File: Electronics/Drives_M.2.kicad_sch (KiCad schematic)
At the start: 87 parts, among them IC3 LM61480Q3RPHRQ1, J14 Bus_M.2_Socket_M, J15 Bus_M.2_Socket_M, J16 Bus_M.2_Socket_M, J17 Bus_M.2_Socket_M, M1 M.2 Screw, M10 M.2 Solder Nut, M11 M.2 Screw, M12 M.2 Screw, M13 M.2 Solder Nut, M14 M.2 Solder Nut, M15 M.2 Solder Nut, M16 M.2 Solder Nut, M17 M.2 Solder Nut, M18 M.2 Solder Nut, M19 M.2 Solder Nut, M2 M.2 Screw, M20 M.2 Solder Nut, M3 M.2 Solder Nut, M4 M.2 Solder Nut, M5 M.2 Solder Nut, M6 M.2 Solder Nut, M7 M.2 Solder Nut, M8 M.2 Solder Nut, M9 M.2 Solder Nut, U7 ASEK-32.768KHZ-L-R-T, U8 ASM1184

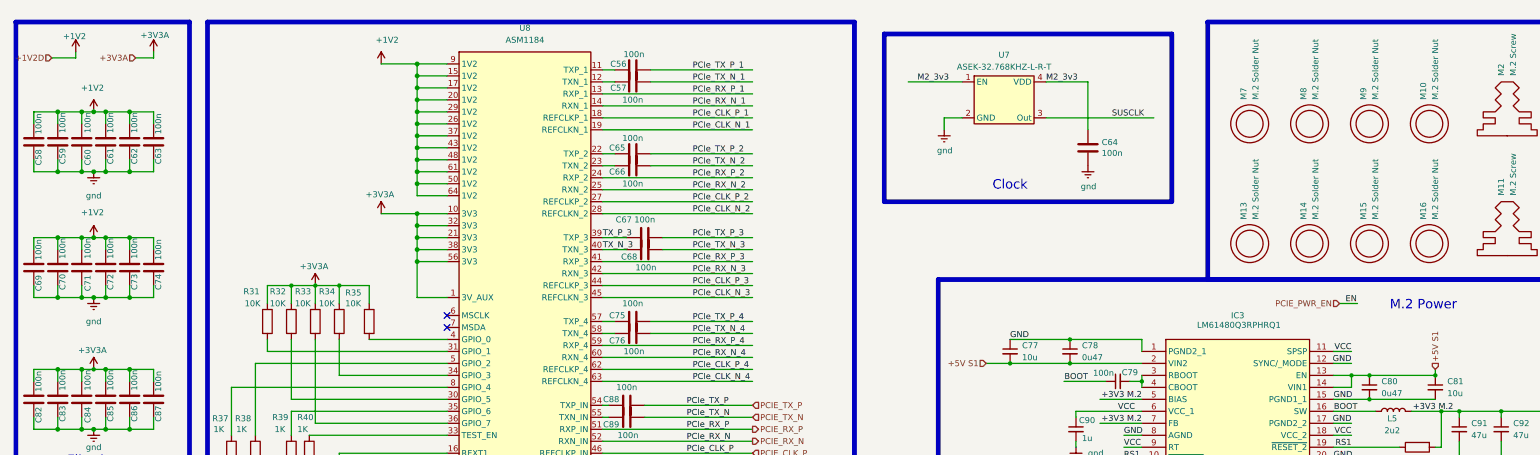
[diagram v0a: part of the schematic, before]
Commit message: Power symbols changed and sata hub fixed schem
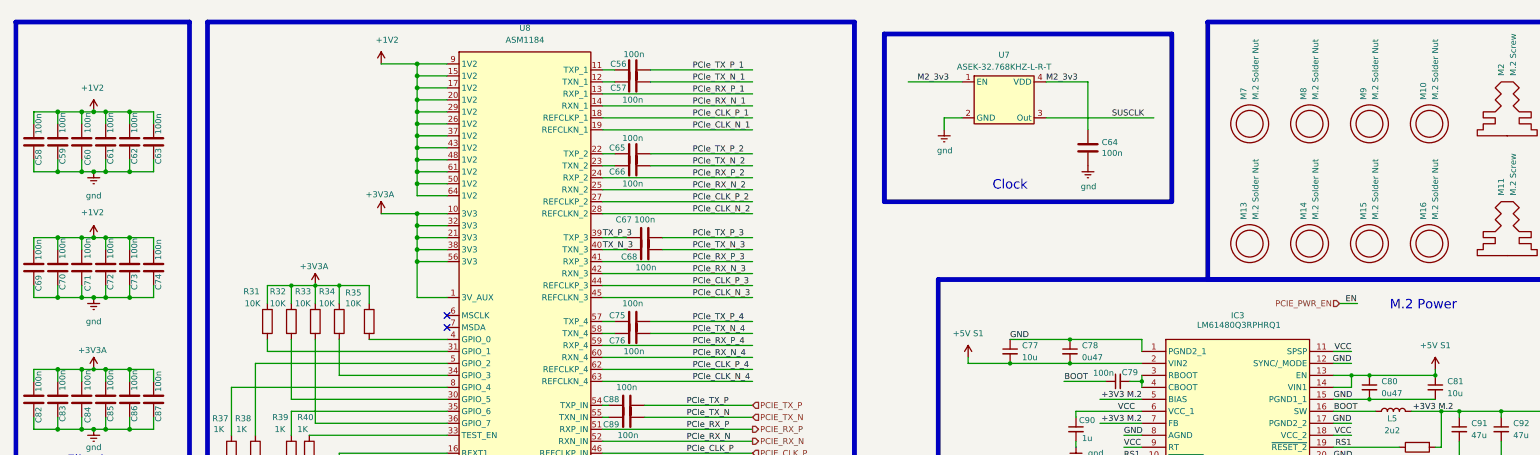
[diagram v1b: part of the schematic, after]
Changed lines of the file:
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@@
 	(wire
 		(pts
-			(xy 38.1 21.59) (xy 41.91 21.59)
-		)
-		(stroke
-			(width 0)
-			(type default)
-		)
-	)
-	(wire
-		(pts
 			(xy 87.63 81.28) (xy 104.14 81.28)
 		)
@@
 	(wire
 		(pts
-			(xy 25.4 21.59) (xy 25.4 20.32)
-		)
-		(stroke
-			(width 0)
-			(type default)
-		)
-	)
-	(wire
-		(pts
 			(xy 125.73 144.78) (xy 138.43 144.78)
 		)
@@
 	(wire
 		(pts
-			(xy 41.91 21.59) (xy 41.91 20.32)
+			(xy 137.16 67.31) (xy 168.91 67.31)
 		)
 		(stroke
@@
 	(wire
 		(pts
-			(xy 137.16 67.31) (xy 168.91 67.31)
+			(xy 214.63 85.09) (xy 214.63 86.36)
 		)
 		(stroke
@@
 	(wire
 		(pts
+			(xy 214.63 86.36) (xy 223.52 86.36)
+		)
+		(stroke
+			(width 0)
+			(type default)
+		)
+	)
+	(wire
+		(pts
 			(xy 223.52 81.28) (xy 236.22 81.28)
 		)
@@
 	(wire
 		(pts
-			(xy 20.32 21.59) (xy 25.4 21.59)
-		)
-		(stroke
-			(width 0)
-			(type default)
-		)
-	)
-	(wire
-		(pts
 			(xy 81.28 116.84) (xy 81.28 115.57)
 		)
@@
 	(wire
 		(pts
-			(xy 218.44 86.36) (xy 223.52 86.36)
-		)
-		(stroke
-			(width 0)
-			(type default)
-		)
-	)
-	(wire
-		(pts
 			(xy 125.73 162.56) (xy 138.43 162.56)
 		)
@@
 		)
 	)
-	(hierarchical_label "+3V3A"
-		(shape input)
-		(at 38.1 21.59 180)
-		(effects
-			(font
-				(size 1.27 1.27)
-			)
-			(justify right)
-		)
-	)
 	(hierarchical_label "PCIE_nCLKREQ"
 		(shape bidirectional)
@@
 		)
 	)
-	(hierarchical_label "+5V S1"
-		(shape input)
-		(at 313.69 87.63 90)
-		(effects
-			(font
-				(size 1.27 1.27)
-			)
-			(justify left)
-		)
-	)
 	(hierarchical_label "PCIE_nWAKE"
 		(shape bidirectional)
@@
 		)
 	)
-	(hierarchical_label "+5V S1"
-		(shape input)
-		(at 218.44 86.36 180)
-		(effects
-			(font
-				(size 1.27 1.27)
-			)
-			(justify right)
-		)
-	)
 	(hierarchical_label "PCIE_nWAKE"
 		(shape bidirectional)
@@
 		)
 	)
-	(hierarchical_label "+1V2D"
-		(shape input)
-		(at 20.32 21.59 180)
-		(effects
-			(font
-				(size 1.27 1.27)
-			)
-			(justify right)
-		)
-	)
 	(rule_area
 		(polyline
@@
 	)
 	(symbol
+		(lib_id "power:+5V")
+		(at 214.63 85.09 0)
+		(unit 1)
+		(exclude_from_sim no)
+		(in_bom yes)
+		(on_board yes)
+		(dnp no)
+		(fields_autoplaced yes)
+		(property "Reference" "#PWR051"
+			(at 214.63 88.9 0)
+			(effects
+				(font
+					(size 1.27 1.27)
+				)
+				(hide yes)
+			)
+		)
+		(property "Value" "+5V S1"
+			(at 214.63 80.01 0)
+			(effects
+				(font
+					(size 1.27 1.27)
+				)
+			)
+		)
+		(property "Footprint" ""
+			(at 214.63 85.09 0)
+			(effects
+				(font
+					(size 1.27 1.27)
+				)
+				(hide yes)
+			)
+		)
+		(property "Datasheet" ""
+			(at 214.63 85.09 0)
+			(effects
+				(font
+					(size 1.27 1.27)
+				)
+				(hide yes)
+			)
+		)
+		(property "Description" "Power symbol creates a global label with name \"+5V\""
+			(at 214.63 85.09 0)
+			(effects
+				(font
+					(size 1.27 1.27)
+				)
+				(hide yes)
+			)
+		)
+		(pin "1"
+		)
+		(instances
+			(project "CM5 Nas"
+				(path "/0650c7a8-acba-429c-9f8e-eec0baf0bc1c/fede4c36-00cc-4d3d-b71c-5243ba232202/3838f96b-aabd-4e80-8b25-6301712882d2"
+					(reference "#PWR051")
+					(unit 1)
+				)
+			)
+		)
+	)
+	(symbol
 		(lib_id "power:Earth")
 		(at 67.31 110.49 0)
@@
 	)
 	(symbol
-		(lib_id "power:+1V2")
-		(at 25.4 20.32 0)
-		(unit 1)
-		(exclude_from_sim no)
-		(in_bom yes)
-		(on_board yes)
-		(dnp no)
-		(property "Reference" "#PWR051"
-			(at 25.4 24.13 0)
-			(effects
-				(font
-					(size 1.27 1.27)
-				)
-				(hide yes)
-			)
-		)
-		(property "Value" "+1V2"
-			(at 25.146 17.018 0)
-			(effects
-				(font
-					(size 1.27 1.27)
-				)
-			)
-		)
-		(property "Footprint" ""
-			(at 25.4 20.32 0)
-			(effects
-				(font
-					(size 1.27 1.27)
-				)
-				(hide yes)
-			)
-		)
-		(property "Datasheet" ""
-			(at 25.4 20.32 0)
-			(effects
-				(font
-					(size 1.27 1.27)
-				)
-				(hide yes)
-			)
-		)
-		(property "Description" ""
-			(at 25.4 20.32 0)
-			(effects
-				(font
-					(size 1.27 1.27)
-				)
-			)
-		)
-		(pin "1"
-		)
-		(instances
-			(project "CM5 Nas"
-				(path "/0650c7a8-acba-429c-9f8e-eec0baf0bc1c/fede4c36-00cc-4d3d-b71c-5243ba232202/3838f96b-aabd-4e80-8b25-6301712882d2"
-					(reference "#PWR051")
-					(unit 1)
-				)
-			)
-		)
-	)
-	(symbol
 		(lib_id "Device:C")
 		(at 21.59 93.98 0)
@@
 	)
 	(symbol
+		(lib_id "power:+5V")
+		(at 313.69 87.63 0)
+		(unit 1)
+		(exclude_from_sim no)
+		(in_bom yes)
+		(on_board yes)
+		(dnp no)
+		(fields_autoplaced yes)
+		(property "Reference" "#PWR052"
+			(at 313.69 91.44 0)
+			(effects
+				(font
+					(size 1.27 1.27)
+				)
+				(hide yes)
+			)
+		)
+		(property "Value" "+5V S1"
+			(at 313.69 82.55 0)
+			(effects
+				(font
+					(size 1.27 1.27)
+				)
+			)
+		)
+		(property "Footprint" ""
+			(at 313.69 87.63 0)
+			(effects
+				(font
+					(size 1.27 1.27)
+				)
+				(hide yes)
+			)
+		)
+		(property "Datasheet" ""
+			(at 313.69 87.63 0)
+			(effects
+				(font
+					(size 1.27 1.27)
+				)
+				(hide yes)
+			)
+		)
+		(property "Description" "Power symbol creates a global label with name \"+5V\""
+			(at 313.69 87.63 0)
+			(effects
+				(font
+					(size 1.27 1.27)
+				)
+				(hide yes)
+			)
+		)
+		(pin "1"
+		)
+		(instances
+			(project "CM5 Nas"
+				(path "/0650c7a8-acba-429c-9f8e-eec0baf0bc1c/fede4c36-00cc-4d3d-b71c-5243ba232202/3838f96b-aabd-4e80-8b25-6301712882d2"
+					(reference "#PWR052")
+					(unit 1)
+				)
+			)
+		)
+	)
+	(symbol
 		(lib_id "Device:C_Small")
 		(at 246.38 90.17 90)
@@
 					(unit 1)
 				)
-			)
-		)
-	)
-	(symbol
-		(lib_id "power:+3.3VA")
-		(at 41.91 20.32 0)
-		(unit 1)
-		(exclude_from_sim no)
-		(in_bom yes)
-		(on_board yes)
-		(dnp no)
-		(property "Reference" "#PWR052"
-			(at 41.91 24.13 0)
-			(effects
-				(font
-					(size 1.27 1.27)
-				)
-				(hide yes)
-			)
-		)
-		(property "Value" "+3V3A"
-			(at 42.164 16.764 0)
-			(effects
-				(font
-					(size 1.27 1.27)
-				)
-			)
-		)
-		(property "Footprint" ""
-			(at 41.91 20.32 0)
-			(effects
-				(font
-					(size 1.27 1.27)
-				)
-				(hide yes)
-			)
-		)
-		(property "Datasheet" ""
-			(at 41.91 20.32 0)
-			(effects
-				(font
-					(size 1.27 1.27)
-				)
-				(hide yes)
-			)
-		)
-		(property "Description" ""
-			(at 41.91 20.32 0)
-			(effects
-				(font
-					(size 1.27 1.27)
-				)
-			)
-		)
-		(pin "1"
-		)
-		(instances
-			(project "CM5 Nas"
-				(path "/0650c7a8-acba-429c-9f8e-eec0baf0bc1c/fede4c36-00cc-4d3d-b71c-5243ba232202/3838f96b-aabd-4e80-8b25-6301712882d2"
-					(reference "#PWR052")
-					(unit 1)
-				)
